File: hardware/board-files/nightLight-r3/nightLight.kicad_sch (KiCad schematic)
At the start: 41 parts, among them IC1 PAM2401SCADJ, IC2 MCP73123T-22SI_MF, J1 USB_C_Receptacle_PowerOnly_6P, J2 Conn_01x03, J3 Conn_01x03, J4 Conn_01x03, J5 Conn_01x03, J6 Conn_01x05_Pin, SW1 TILT, U2 ATtiny1614-SS

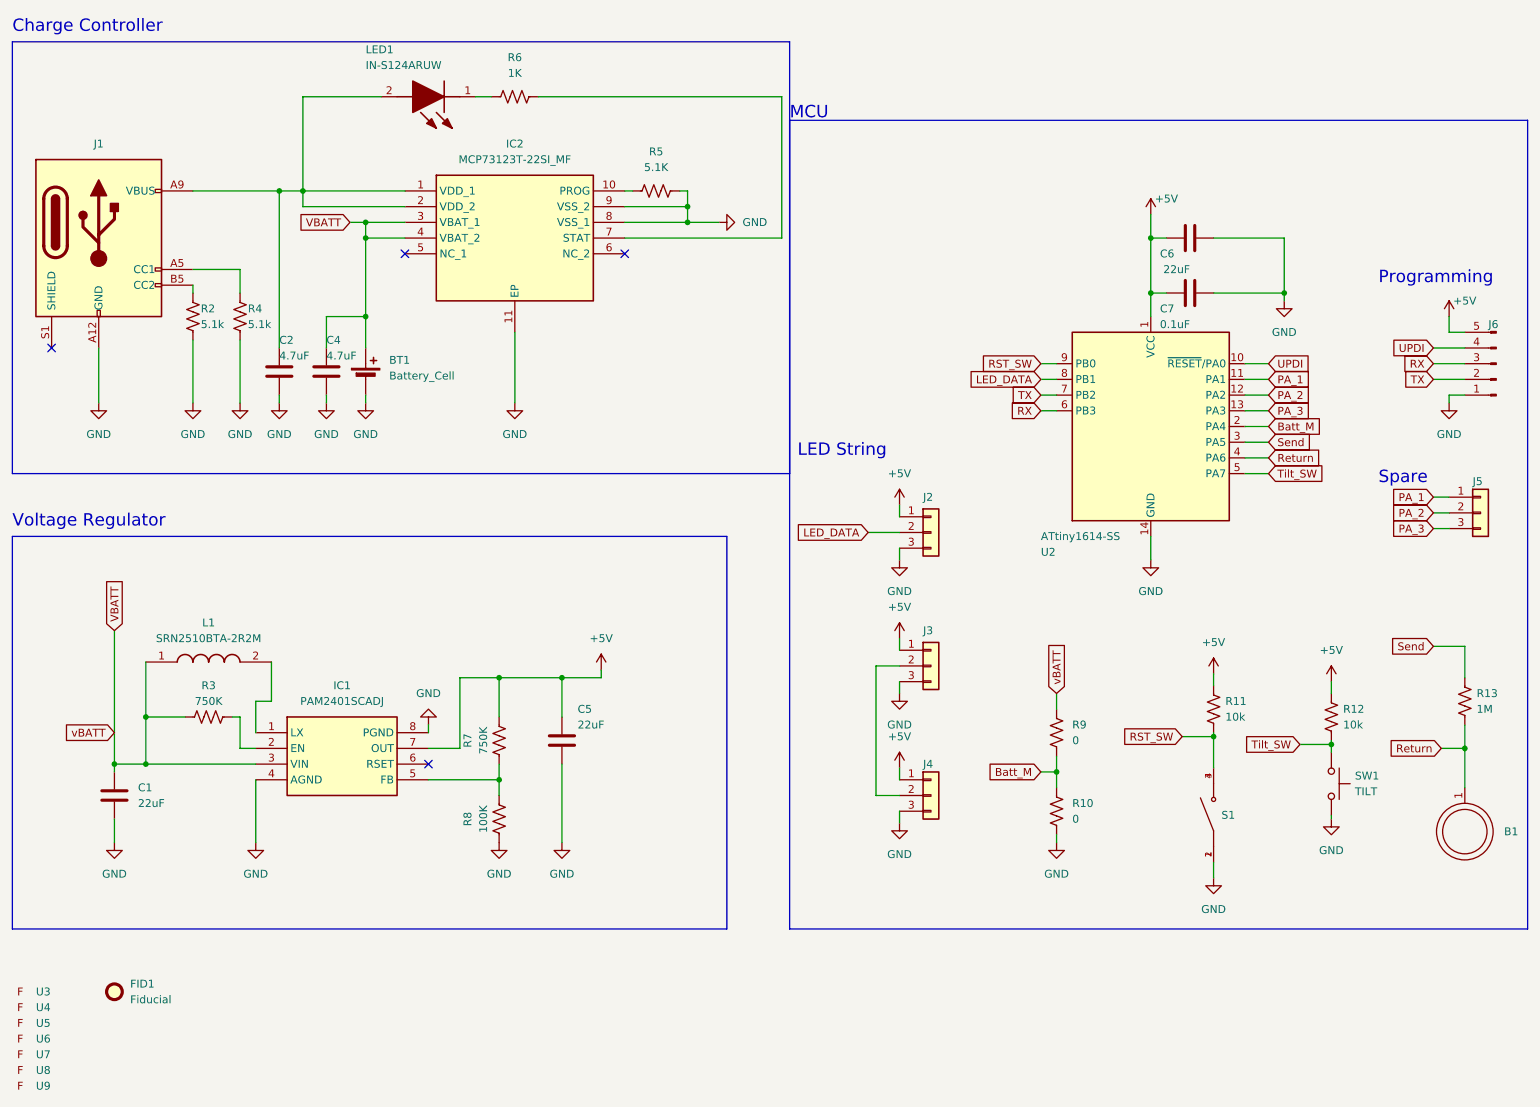
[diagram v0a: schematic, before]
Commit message: Added LCD cct and broke schematics into different sheets
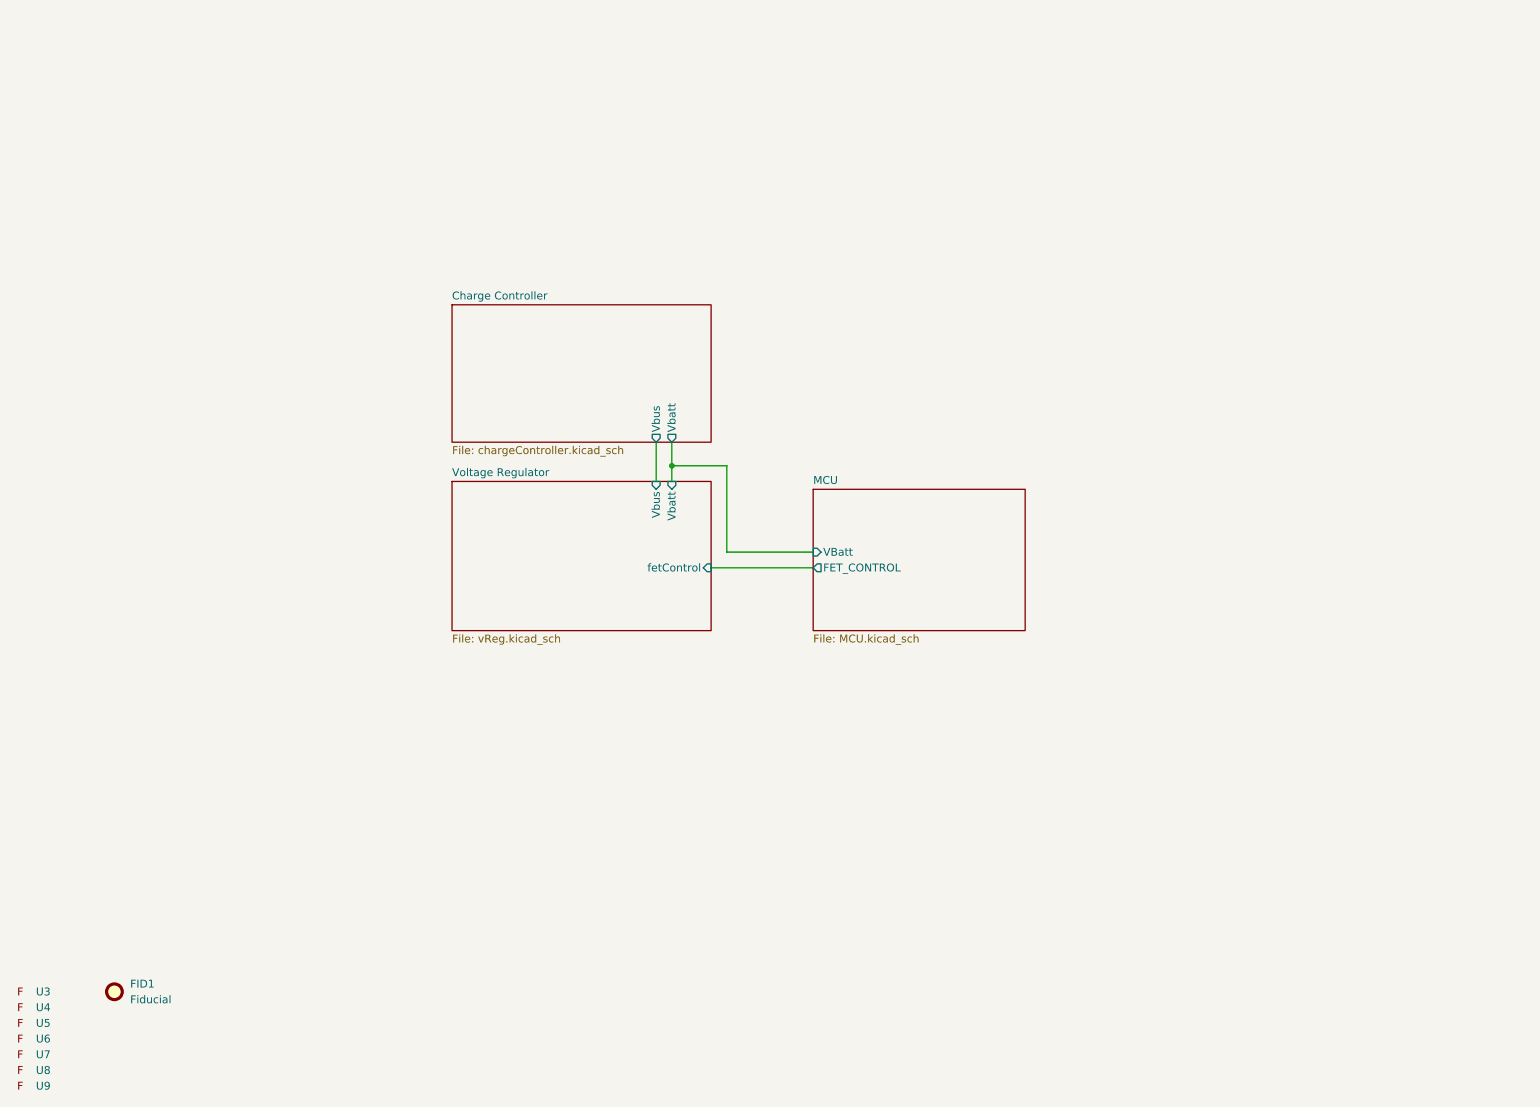
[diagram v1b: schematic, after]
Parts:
- removed B1: ~, myFootprintDesigns:fireflyTouch, symbol myDesigns:Touch_Button
- removed BT1: Battery_Cell, myFootprintDesigns:14500 Holder, symbol Device:Battery_Cell
- removed C1, C5, C6: 22uF, Capacitor_SMD:C_0805_2012Metric, symbol Device:C
- removed C2, C4: 4.7uF, Capacitor_SMD:C_0805_2012Metric, symbol Device:C
- removed C7: 0.1uF, Capacitor_SMD:C_0805_2012Metric, symbol Device:C
- removed IC1: PAM2401SCADJ, PAM2401:SOP65P490X110-8N, symbol PAM2401SCADJ:PAM2401SCADJ
- removed IC2: MCP73123T-22SI_MF, MCP73123T-22SI_MF:SON50P300X300X100-11N-D, symbol MCP73123T-22SI_MF:MCP73123T-22SI_MF
- removed J1: USB_C_Receptacle_PowerOnly_6P, myFootprintDesigns:USB-C_PWR, symbol Connector:USB_C_Receptacle_PowerOnly_6P
- removed J2, J3, J4: Conn_01x03, Connector_PinHeader_2.54mm:PinHeader_1x03_P2.54mm_Vertical_SMD_Pin1Left, symbol Connector_Generic:Conn_01x03
- removed J5: Conn_01x03, myFootprintDesigns:spares_1*3, symbol Connector_Generic:Conn_01x03
- removed J6: Conn_01x05_Pin, Connector_PinSocket_2.54mm:PinSocket_1x05_P2.54mm_Vertical_SMD_Pin1Left, symbol Connector:Conn_01x05_Pin
- removed L1: SRN2510BTA-2R2M, SRN2510BTA-2R2M:SRN2510BTA2R2M, symbol SRN2510BTA-2R2M:SRN2510BTA-2R2M
- removed LED1: IN-S124ARUW, KiCad-SMTLED:INS124ARUW, symbol newIN-S124ARUW:IN-S124ARUW
- removed R10, R9: 0, Resistor_SMD:R_0805_2012Metric, symbol Device:R_US
- removed R11, R12: 10k, Resistor_SMD:R_0805_2012Metric, symbol Device:R_US
- removed R13: 1M, Resistor_SMD:R_0805_2012Metric, symbol Device:R_US
- removed R2, R4: 5.1k, Resistor_SMD:R_0805_2012Metric, symbol Device:R_US
- removed R3, R7: 750K, Resistor_SMD:R_0805_2012Metric, symbol Device:R_US
- removed R5: 5.1K, Resistor_SMD:R_0805_2012Metric, symbol Device:R_US
- removed R6: 1K, Resistor_SMD:R_0805_2012Metric, symbol Device:R_US
- removed R8: 100K, Resistor_SMD:R_0805_2012Metric, symbol Device:R_US
- removed S1: PTS526_SM08_SMTR2_LFS, PTS526_SM08_SMTR2_LFS:SW_PTS526_SM08_SMTR2_LFS, symbol PTS526_SM08_SMTR2_LFS:PTS526_SM08_SMTR2_LFS
- removed SW1: TILT, Connector_PinHeader_2.54mm:PinHeader_2x01_P2.54mm_Vertical_SMD, symbol Switch:SW_Push
- removed U2: ATtiny1614-SS, Package_SO:SOIC-14_3.9x8.7mm_P1.27mm, symbol MCU_Microchip_ATtiny:ATtiny1614-SS
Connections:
- no-connect marks 4 -> 0
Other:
- added sheet Charge Controller (chargeController.kicad_sch)
- added sheet MCU (MCU.kicad_sch)
- added sheet Voltage Regulator (vReg.kicad_sch)
- note removed: "Charge Controller"
- note removed: "LED String"
- note removed: "MCU"
- note removed: "Programming"
- note removed: "Spare"
- note removed: "Voltage Regulator"

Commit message: first layout revision
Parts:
- renumbered U3 to U1, U4 to U2, U5 to U3, U6 to U4, U7 to U5, U8 to U6, U9 to U7
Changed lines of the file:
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@@
   (symbol (lib_id "myDesigns:Firefly_Symbol") (at 25.4 189.23 0) (unit 1)
     (in_bom yes) (on_board yes) (dnp no) (fields_autoplaced)
-    (property "Reference" "U9" (at 29.21 187.96 0)
+    (property "Reference" "U7" (at 29.21 187.96 0)
       (effects (font (size 1.27 1.27)) (justify left))
     )
@@
       (project "nightLight"
         (path "/203033dd-6a13-4262-9a98-8b29445e90e8"
-          (reference "U9") (unit 1)
+          (reference "U7") (unit 1)
         )
       )
@@
   (symbol (lib_id "myDesigns:Firefly_Symbol") (at 25.4 186.69 0) (unit 1)
     (in_bom yes) (on_board yes) (dnp no) (fields_autoplaced)
-    (property "Reference" "U8" (at 29.21 185.42 0)
+    (property "Reference" "U6" (at 29.21 185.42 0)
       (effects (font (size 1.27 1.27)) (justify left))
     )
@@
       (project "nightLight"
         (path "/203033dd-6a13-4262-9a98-8b29445e90e8"
-          (reference "U8") (unit 1)
+          (reference "U6") (unit 1)
         )
       )
@@
   (symbol (lib_id "myDesigns:Firefly_Symbol") (at 25.4 181.61 0) (unit 1)
     (in_bom yes) (on_board yes) (dnp no) (fields_autoplaced)
-    (property "Reference" "U6" (at 29.21 180.34 0)
+    (property "Reference" "U4" (at 29.21 180.34 0)
       (effects (font (size 1.27 1.27)) (justify left))
     )
@@
       (project "nightLight"
         (path "/203033dd-6a13-4262-9a98-8b29445e90e8"
-          (reference "U6") (unit 1)
+          (reference "U4") (unit 1)
         )
       )
@@
   (symbol (lib_id "myDesigns:Firefly_Symbol") (at 25.4 179.07 0) (unit 1)
     (in_bom yes) (on_board yes) (dnp no) (fields_autoplaced)
-    (property "Reference" "U5" (at 29.21 177.8 0)
+    (property "Reference" "U3" (at 29.21 177.8 0)
       (effects (font (size 1.27 1.27)) (justify left))
     )
@@
       (project "nightLight"
         (path "/203033dd-6a13-4262-9a98-8b29445e90e8"
-          (reference "U5") (unit 1)
+          (reference "U3") (unit 1)
         )
       )
@@
   (symbol (lib_id "myDesigns:Firefly_Symbol") (at 25.4 176.53 0) (unit 1)
     (in_bom yes) (on_board yes) (dnp no) (fields_autoplaced)
-    (property "Reference" "U4" (at 29.21 175.26 0)
+    (property "Reference" "U2" (at 29.21 175.26 0)
       (effects (font (size 1.27 1.27)) (justify left))
     )
@@
       (project "nightLight"
         (path "/203033dd-6a13-4262-9a98-8b29445e90e8"
-          (reference "U4") (unit 1)
+          (reference "U2") (unit 1)
         )
       )
@@
   (symbol (lib_id "myDesigns:Firefly_Symbol") (at 25.4 173.99 0) (unit 1)
     (in_bom yes) (on_board yes) (dnp no) (fields_autoplaced)
-    (property "Reference" "U3" (at 29.21 172.72 0)
+    (property "Reference" "U1" (at 29.21 172.72 0)
       (effects (font (size 1.27 1.27)) (justify left))
     )
@@
       (project "nightLight"
         (path "/203033dd-6a13-4262-9a98-8b29445e90e8"
-          (reference "U3") (unit 1)
+          (reference "U1") (unit 1)
         )
       )
@@
   (symbol (lib_id "myDesigns:Firefly_Symbol") (at 25.4 184.15 0) (unit 1)
     (in_bom yes) (on_board yes) (dnp no) (fields_autoplaced)
-    (property "Reference" "U7" (at 29.21 182.88 0)
+    (property "Reference" "U5" (at 29.21 182.88 0)
       (effects (font (size 1.27 1.27)) (justify left))
     )
@@
       (project "nightLight"
         (path "/203033dd-6a13-4262-9a98-8b29445e90e8"
-          (reference "U7") (unit 1)
+          (reference "U5") (unit 1)
         )
       )
